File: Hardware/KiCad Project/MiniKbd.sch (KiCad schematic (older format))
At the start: 18 parts, among them IC1 Trinket3v3, SW1 SPST, SW2 SPST, SW3 SPST, SW4 SPST, SW5 SPST, SW6 SPST

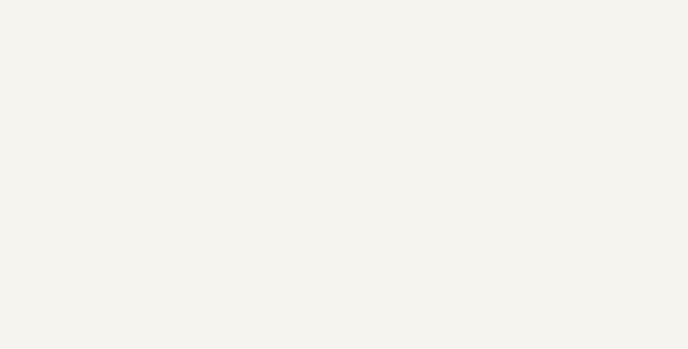
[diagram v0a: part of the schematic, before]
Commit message: Added schematic PDF
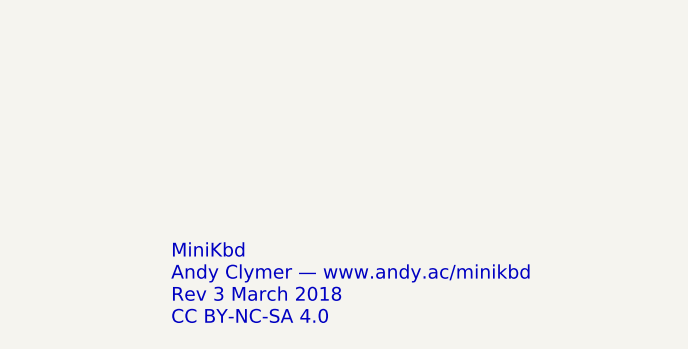
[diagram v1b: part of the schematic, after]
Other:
- note added: "MiniKbd\nAndy Clymer — www.andy.ac/minikbd\nRev 3 March 2018\nCC BY-NC-SA 4.0"
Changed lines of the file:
@@
 Wire Wire Line
 	8400 4400 8550 4400
+Text Notes 7050 7050 0    60   ~ 0
+MiniKbd\nAndy Clymer — www.andy.ac/minikbd\nRev 3 March 2018\nCC BY-NC-SA 4.0
 $EndSCHEMATC
